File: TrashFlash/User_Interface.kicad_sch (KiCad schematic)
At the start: 15 parts, among them IC601 LP5024RSMR

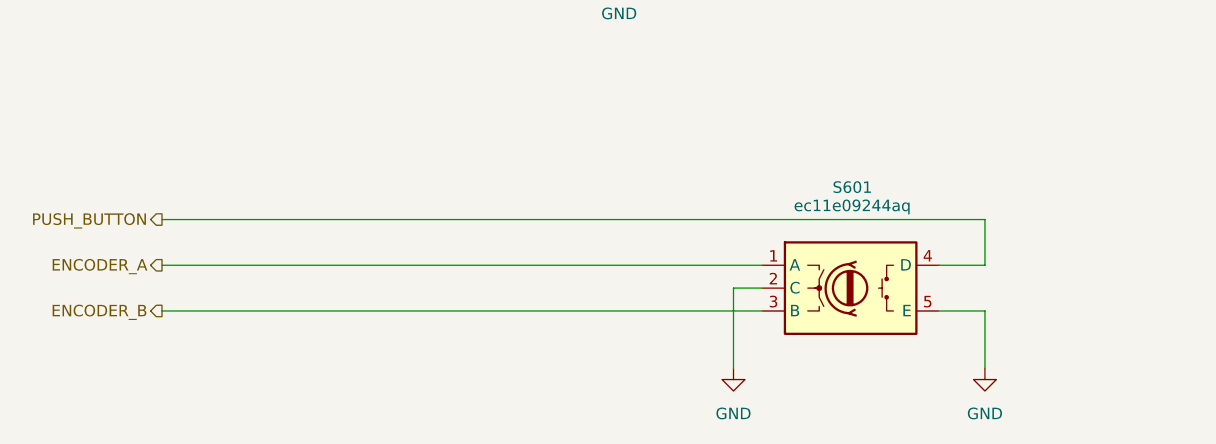
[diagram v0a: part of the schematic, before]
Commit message: Stackup changed, Led placement adjusted
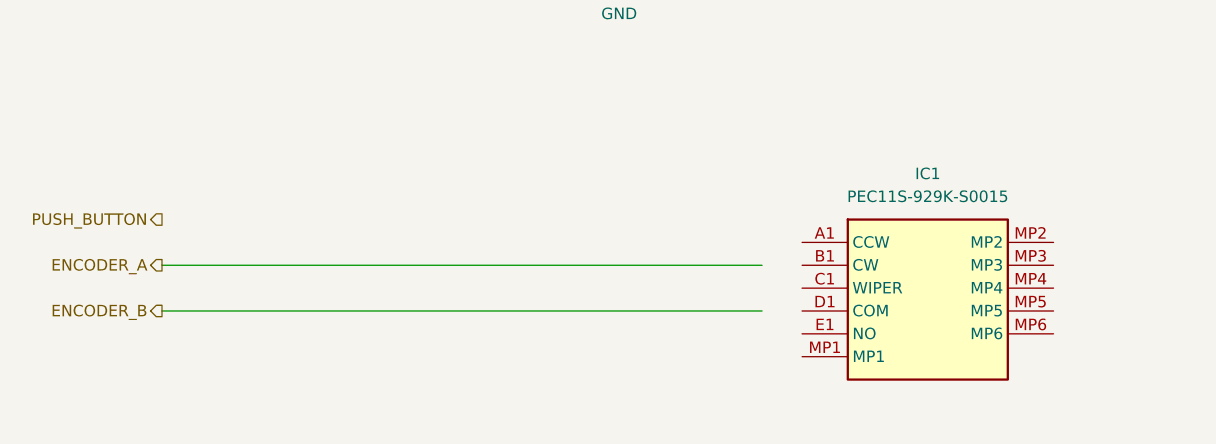
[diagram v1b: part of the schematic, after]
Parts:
- removed S601: ec11e09244aq, ec11e09244aq, symbol TrashFlash:ec11e09244aq
- added IC1: PEC11S-929K-S0015, PEC11S929KS0015, symbol TrashFlash:PEC11S-929K-S0015
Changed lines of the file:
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@@
 	(wire
 		(pts
-			(xy 76.2 146.05) (xy 167.64 146.05)
-		)
-		(stroke
-			(width 0)
-			(type default)
-		)
-	)
-	(wire
-		(pts
 			(xy 238.76 71.12) (xy 241.3 71.12)
 		)
@@
 	(wire
 		(pts
-			(xy 167.64 146.05) (xy 167.64 151.13)
-		)
-		(stroke
-			(width 0)
-			(type default)
-		)
-	)
-	(wire
-		(pts
 			(xy 213.36 86.36) (xy 215.9 86.36)
 		)
@@
 	(wire
 		(pts
-			(xy 142.875 153.67) (xy 139.7 153.67)
-		)
-		(stroke
-			(width 0)
-			(type default)
-		)
-	)
-	(wire
-		(pts
 			(xy 213.36 66.04) (xy 215.9 66.04)
 		)
@@
 	(wire
 		(pts
-			(xy 167.64 151.13) (xy 162.56 151.13)
-		)
-		(stroke
-			(width 0)
-			(type default)
-		)
-	)
-	(wire
-		(pts
 			(xy 114.3 50.8) (xy 114.3 63.5)
 		)
@@
 	(wire
 		(pts
-			(xy 167.64 156.21) (xy 167.64 162.56)
-		)
-		(stroke
-			(width 0)
-			(type default)
-		)
-	)
-	(wire
-		(pts
-			(xy 162.56 156.21) (xy 167.64 156.21)
-		)
-		(stroke
-			(width 0)
-			(type default)
-		)
-	)
-	(wire
-		(pts
 			(xy 198.12 83.82) (xy 170.18 83.82)
 		)
@@
 	(wire
 		(pts
-			(xy 139.7 153.67) (xy 139.7 162.56)
-		)
-		(stroke
-			(width 0)
-			(type default)
-		)
-	)
-	(wire
-		(pts
 			(xy 215.9 81.28) (xy 241.3 81.28)
 		)
@@
 	)
 	(symbol
-		(lib_id "TrashFlash:ec11e09244aq")
-		(at 142.875 151.13 0)
-		(unit 1)
-		(exclude_from_sim no)
-		(in_bom yes)
-		(on_board yes)
-		(dnp no)
-		(property "Reference" "S601"
-			(at 152.908 142.494 0)
-			(effects
-				(font
-					(size 1.27 1.27)
-				)
-			)
-		)
-		(property "Value" "ec11e09244aq"
-			(at 152.908 144.526 0)
-			(effects
-				(font
-					(size 1.27 1.27)
-				)
-			)
-		)
-		(property "Footprint" "ec11e09244aq"
-			(at 142.875 151.13 0)
-			(effects
-				(font
-					(size 1.27 1.27)
-				)
-				(hide yes)
-			)
-		)
-		(property "Datasheet" "https://eu.mouser.com/datasheet/2/15/alps_alps-s-a0008379064-1-1733314.pdf"
-			(at 142.875 151.13 0)
-			(effects
-				(font
-					(size 1.27 1.27)
-				)
-				(hide yes)
-			)
-		)
-		(property "Description" ""
-			(at 142.875 151.13 0)
-			(effects
-				(font
-					(size 1.27 1.27)
-				)
-				(hide yes)
-			)
-		)
-		(pin "4"
-		)
-		(pin "2"
-		)
-		(pin "3"
-		)
-		(pin "5"
-		)
-		(pin "1"
-		)
-		(instances
-			(project ""
-				(path "/256082dc-9c82-41ae-bfb7-0b4bd4121c78/fa02bcf9-bdc6-4000-b431-14bacede6ea5"
-					(reference "S601")
-					(unit 1)
-				)
-			)
-		)
-	)
-	(symbol
 		(lib_id "TrashFlash:LP5024RSMR")
 		(at 139.7 38.1 0)
@@
 	)
 	(symbol
+		(lib_id "TrashFlash:PEC11S-929K-S0015")
+		(at 147.32 148.59 0)
+		(unit 1)
+		(exclude_from_sim no)
+		(in_bom yes)
+		(on_board yes)
+		(dnp no)
+		(fields_autoplaced yes)
+		(property "Reference" "IC1"
+			(at 161.29 140.97 0)
+			(effects
+				(font
+					(size 1.27 1.27)
+				)
+			)
+		)
+		(property "Value" "PEC11S-929K-S0015"
+			(at 161.29 143.51 0)
+			(effects
+				(font
+					(size 1.27 1.27)
+				)
+			)
+		)
+		(property "Footprint" "PEC11S929KS0015"
+			(at 171.45 243.51 0)
+			(effects
+				(font
+					(size 1.27 1.27)
+				)
+				(justify left top)
+				(hide yes)
+			)
+		)
+		(property "Datasheet" "https://componentsearchengine.com/Datasheets/1/PEC11S-929K-S0015.pdf"
+			(at 171.45 343.51 0)
+			(effects
+				(font
+					(size 1.27 1.27)
+				)
+				(justify left top)
+				(hide yes)
+			)
+		)
+		(property "Description" "PEC11S Series - 12 mm SMD Incremental Encoder."
+			(at 147.32 148.59 0)
+			(effects
+				(font
+					(size 1.27 1.27)
+				)
+				(hide yes)
+			)
+		)
+		(property "Height" "14"
+			(at 171.45 543.51 0)
+			(effects
+				(font
+					(size 1.27 1.27)
+				)
+				(justify left top)
+				(hide yes)
+			)
+		)
+		(property "Mouser Part Number" "652-PEC11S929K-S0015"
+			(at 171.45 643.51 0)
+			(effects
+				(font
+					(size 1.27 1.27)
+				)
+				(justify left top)
+				(hide yes)
+			)
+		)
+		(property "Mouser Price/Stock" "https://www.mouser.co.uk/ProductDetail/Bourns/PEC11S-929K-S0015?qs=80T3JVN997A05YR0wgcotA%3D%3D"
+			(at 171.45 743.51 0)
+			(effects
+				(font
+					(size 1.27 1.27)
+				)
+				(justify left top)
+				(hide yes)
+			)
+		)
+		(property "Manufacturer_Name" "Bourns"
+			(at 171.45 843.51 0)
+			(effects
+				(font
+					(size 1.27 1.27)
+				)
+				(justify left top)
+				(hide yes)
+			)
+		)
+		(property "Manufacturer_Part_Number" "PEC11S-929K-S0015"
+			(at 171.45 943.51 0)
+			(effects
+				(font
+					(size 1.27 1.27)
+				)
+				(justify left top)
+				(hide yes)
+			)
+		)
+		(pin "MP5"
+		)
+		(pin "B1"
+		)
+		(pin "A1"
+		)
+		(pin "MP6"
+		)
+		(pin "MP1"
+		)
+		(pin "MP4"
+		)
+		(pin "E1"
+		)
+		(pin "D1"
+		)
+		(pin "MP2"
+		)
+		(pin "MP3"
+		)
+		(pin "C1"
+		)
+		(instances
+			(project ""
+				(path "/256082dc-9c82-41ae-bfb7-0b4bd4121c78/fa02bcf9-bdc6-4000-b431-14bacede6ea5"
+					(reference "IC1")
+					(unit 1)
+				)
+			)
+		)
+	)
+	(symbol
 		(lib_id "power:VDD")
 		(at 109.22 39.37 0)
@@
 	)
 	(symbol
-		(lib_id "power:GND")
-		(at 139.7 162.56 0)
-		(unit 1)
-		(exclude_from_sim no)
-		(in_bom yes)
-		(on_board yes)
-		(dnp no)
-		(fields_autoplaced yes)
-		(property "Reference" "#PWR0607"
-			(at 139.7 168.91 0)
-			(effects
-				(font
-					(size 1.27 1.27)
-				)
-				(hide yes)
-			)
-		)
-		(property "Value" "GND"
-			(at 139.7 167.64 0)
-			(effects
-				(font
-					(size 1.27 1.27)
-				)
-			)
-		)
-		(property "Footprint" ""
-			(at 139.7 162.56 0)
-			(effects
-				(font
-					(size 1.27 1.27)
-				)
-				(hide yes)
-			)
-		)
-		(property "Datasheet" ""
-			(at 139.7 162.56 0)
-			(effects
-				(font
-					(size 1.27 1.27)
-				)
-				(hide yes)
-			)
-		)
-		(property "Description" "Power symbol creates a global label with name \"GND\" , ground"
-			(at 139.7 162.56 0)
-			(effects
-				(font
-					(size 1.27 1.27)
-				)
-				(hide yes)
-			)
-		)
-		(pin "1"
-		)
-		(instances
-			(project "TrashFlash"
-				(path "/256082dc-9c82-41ae-bfb7-0b4bd4121c78/fa02bcf9-bdc6-4000-b431-14bacede6ea5"
-					(reference "#PWR0607")
-					(unit 1)
-				)
-			)
-		)
-	)
-	(symbol
 		(lib_id "TrashFlash:150282M153310")
 		(at 205.74 104.14 0)
@@
 					(unit 1)
 				)
-			)
-		)
-	)
-	(symbol
-		(lib_id "power:GND")
-		(at 167.64 162.56 0)
-		(unit 1)
-		(exclude_from_sim no)
-		(in_bom yes)
-		(on_board yes)
-		(dnp no)
-		(fields_autoplaced yes)
-		(property "Reference" "#PWR0608"
-			(at 167.64 168.91 0)
-			(effects
-				(font
-					(size 1.27 1.27)
-				)
-				(hide yes)
-			)
-		)
-		(property "Value" "GND"
-			(at 167.64 167.64 0)
-			(effects
-				(font
-					(size 1.27 1.27)
-				)
-			)
-		)
-		(property "Footprint" ""
-			(at 167.64 162.56 0)
-			(effects
-				(font
-					(size 1.27 1.27)
-				)
-				(hide yes)
-			)
-		)
-		(property "Datasheet" ""
-			(at 167.64 162.56 0)
-			(effects
-				(font
-					(size 1.27 1.27)
-				)
-				(hide yes)
-			)
-		)
-		(property "Description" "Power symbol creates a global label with name \"GND\" , ground"
-			(at 167.64 162.56 0)
-			(effects
-				(font
-					(size 1.27 1.27)
-				)
-				(hide yes)
-			)
-		)
-		(pin "1"
-		)
-		(instances
-			(project "TrashFlash"
-				(path "/256082dc-9c82-41ae-bfb7-0b4bd4121c78/fa02bcf9-bdc6-4000-b431-14bacede6ea5"
-					(reference "#PWR0608")
-					(unit 1)
-				)

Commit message: Moved USB and added JTAG connector
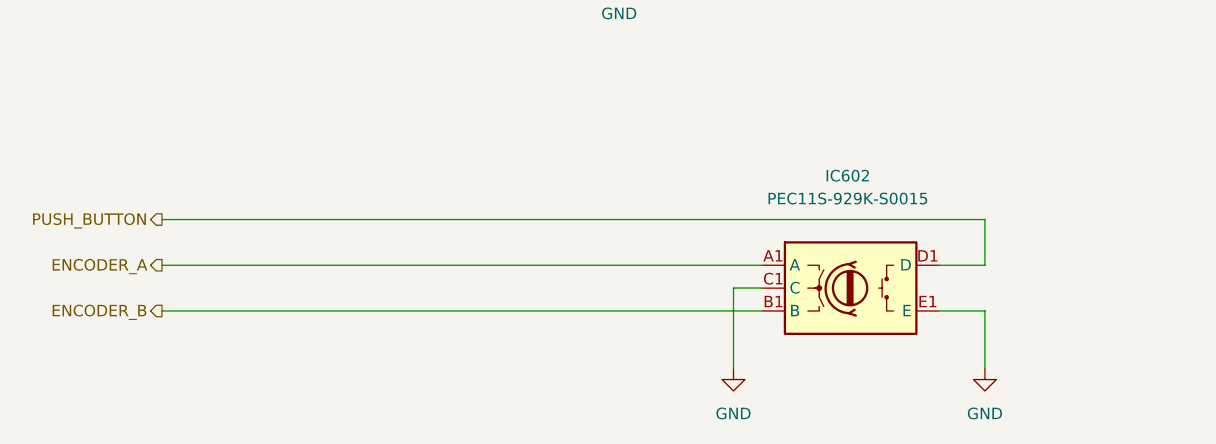
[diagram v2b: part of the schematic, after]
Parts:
- removed IC1: PEC11S-929K-S0015, PEC11S929KS0015, symbol TrashFlash:PEC11S-929K-S0015
- added IC602: PEC11S-929K-S0015, PEC11S929KS0015, symbol TrashFlash:PEC11S-929K-S0015
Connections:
- net ENCODER_A: now also IC602.A1 (A)
- net ENCODER_B: now also IC602.B1 (B)
- net GND: now also IC602.C1 (C), IC602.E1 (E)
- net PUSH_BUTTON: now also IC602.D1 (D)

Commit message: Added battery and connectors, Schematic remark for BQ297xx
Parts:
- IC601: footprint QFN40P400X400X100-33N-D -> TrashFlash:QFN40P400X400X100-33N-D
- IC602: footprint PEC11S929KS0015 -> TrashFlash:PEC11S929KS0015
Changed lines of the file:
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@@
 			)
 		)
-		(property "Footprint" "QFN40P400X400X100-33N-D"
+		(property "Footprint" "TrashFlash:QFN40P400X400X100-33N-D"
 			(at 138.43 127 0)
 			(effects
@@
 			)
 		)
-		(property "Footprint" "PEC11S929KS0015"
+		(property "Footprint" "TrashFlash:PEC11S929KS0015"
 			(at 144.526 161.29 0)
 			(effects
